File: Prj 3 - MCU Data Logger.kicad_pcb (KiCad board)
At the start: 2 copper layers, 0 parts

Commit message: Setup PCB New
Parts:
- added BT1: Battery, Connector_PinHeader_2.54mm:PinHeader_1x02_P2.54mm_Vertical, F.Cu at (154.9, 110.3)
- added C1: 0.1uF, Capacitor_SMD:C_0805_2012Metric, F.Cu at (177.2, 100.1)
- added C2: 22pF, Capacitor_SMD:C_0805_2012Metric, F.Cu at (177.2, 103.1)
- added C3: 22pF, Capacitor_SMD:C_0805_2012Metric, F.Cu at (177.2, 106.1)
- added C4: 0.1uF, Capacitor_SMD:C_0805_2012Metric, F.Cu at (177.2, 109.1)
- added C5: 100nF, Capacitor_SMD:C_0805_2012Metric, F.Cu at (177.2, 112.1)
- added D1: LED, LED_SMD:LED_0805_2012Metric, F.Cu at (181.7, 100.1)
- added D2: LED, LED_SMD:LED_0805_2012Metric, F.Cu at (181.7, 103.1)
- added H1: MountingHole, MountingHole:MountingHole_2.1mm, F.Cu at (155.5, 87.9)
- added H2: MountingHole, MountingHole:MountingHole_2.1mm, F.Cu at (155.5, 93.6)
- added H3: MountingHole, MountingHole:MountingHole_2.1mm, F.Cu at (155.5, 99.4)
- added H4: MountingHole, MountingHole:MountingHole_2.1mm, F.Cu at (155.5, 105.1)
- added J1: Conn_01x04_Pin, Connector_PinHeader_2.54mm:PinHeader_1x04_P2.54mm_Vertical, F.Cu at (192.8, 87.3)
- added J2: Conn_01x09_Pin, Connector_PinHeader_2.54mm:PinHeader_1x09_P2.54mm_Vertical, F.Cu at (188.2, 87.3)
- added J3: Conn_01x04_Pin, Connector_PinHeader_2.54mm:PinHeader_1x04_P2.54mm_Vertical, F.Cu at (197.5, 87.3)
- added J4: Conn_02x03_Odd_Even, Connector_PinHeader_2.54mm:PinHeader_2x03_P2.54mm_Vertical, F.Cu at (192.8, 99.6)
- added R1: 10k, Resistor_SMD:R_0805_2012Metric, F.Cu at (160.5, 86.5)
- added R2: 10k, Resistor_SMD:R_0805_2012Metric, F.Cu at (160.5, 89.4)
- added R3: 4.7k, Resistor_SMD:R_0805_2012Metric, F.Cu at (160.5, 92.4)
- added R4: 4.7k, Resistor_SMD:R_0805_2012Metric, F.Cu at (160.5, 95.3)
- added R5: 330, Resistor_SMD:R_0805_2012Metric, F.Cu at (160.5, 98.3)
- added R6: 10k, Resistor_SMD:R_0805_2012Metric, F.Cu at (160.5, 101.2)
- added R7: 330, Resistor_SMD:R_0805_2012Metric, F.Cu at (160.5, 104.2)
- added U1: 24LC1025, Package_SO:SOIC-8_5.23x5.23mm_P1.27mm, F.Cu at (167.9, 88.4)
- added U2: 24LC1025, Package_SO:SOIC-8_5.23x5.23mm_P1.27mm, F.Cu at (167.9, 95.2)
- added U3: DS1337S_, DS1337S:DS1337S, F.Cu at (167.9, 113.2)
- added U4: ATMEGA328P-AU, ATMEGA328P-AU:ATMEGA328P-AU, F.Cu at (169.3, 104.2)
- added Y1: 32.768 KHz, Crystal:Crystal_SMD_5032-2Pin_5.0x3.2mm_HandSoldering, F.Cu at (178.2, 87.4)
- added Y2: 16MHz, Crystal:Crystal_SMD_5032-2Pin_5.0x3.2mm_HandSoldering, F.Cu at (178.2, 92.3)

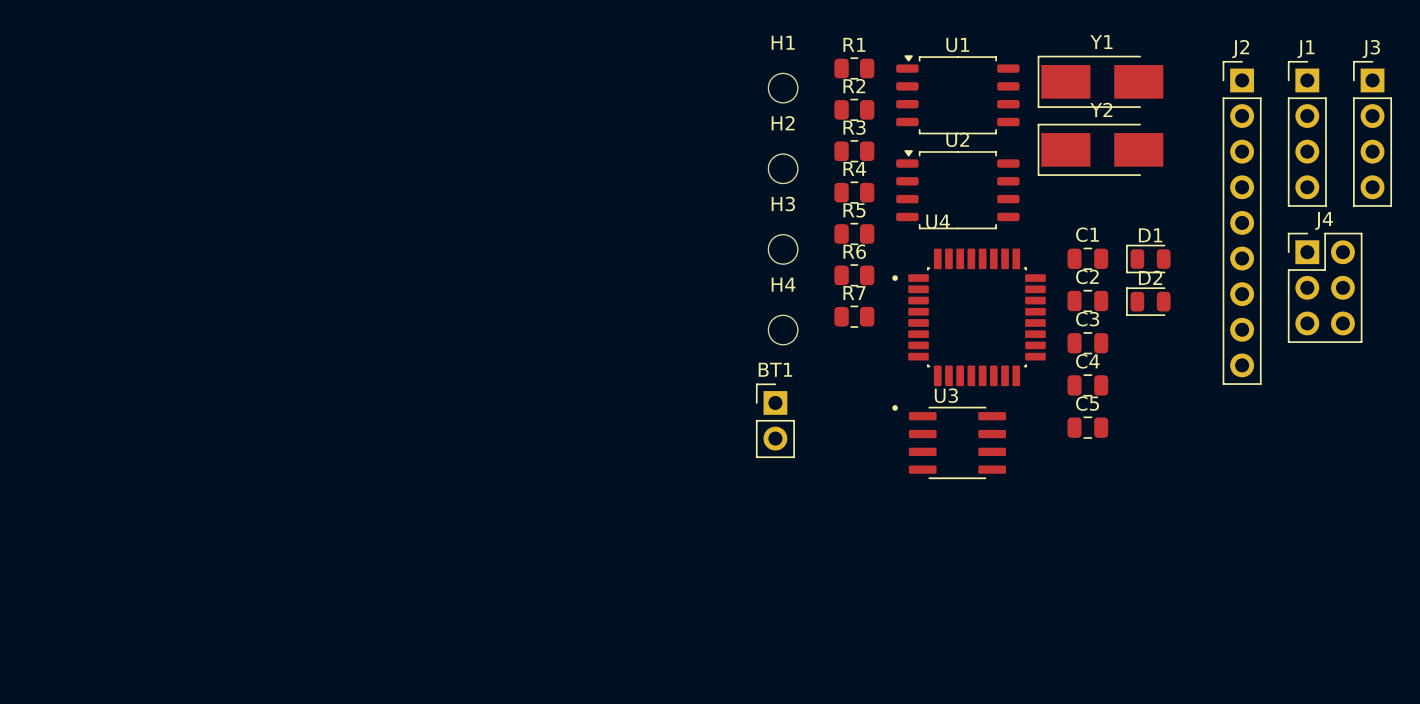
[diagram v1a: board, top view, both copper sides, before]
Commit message: Arranged placeholders
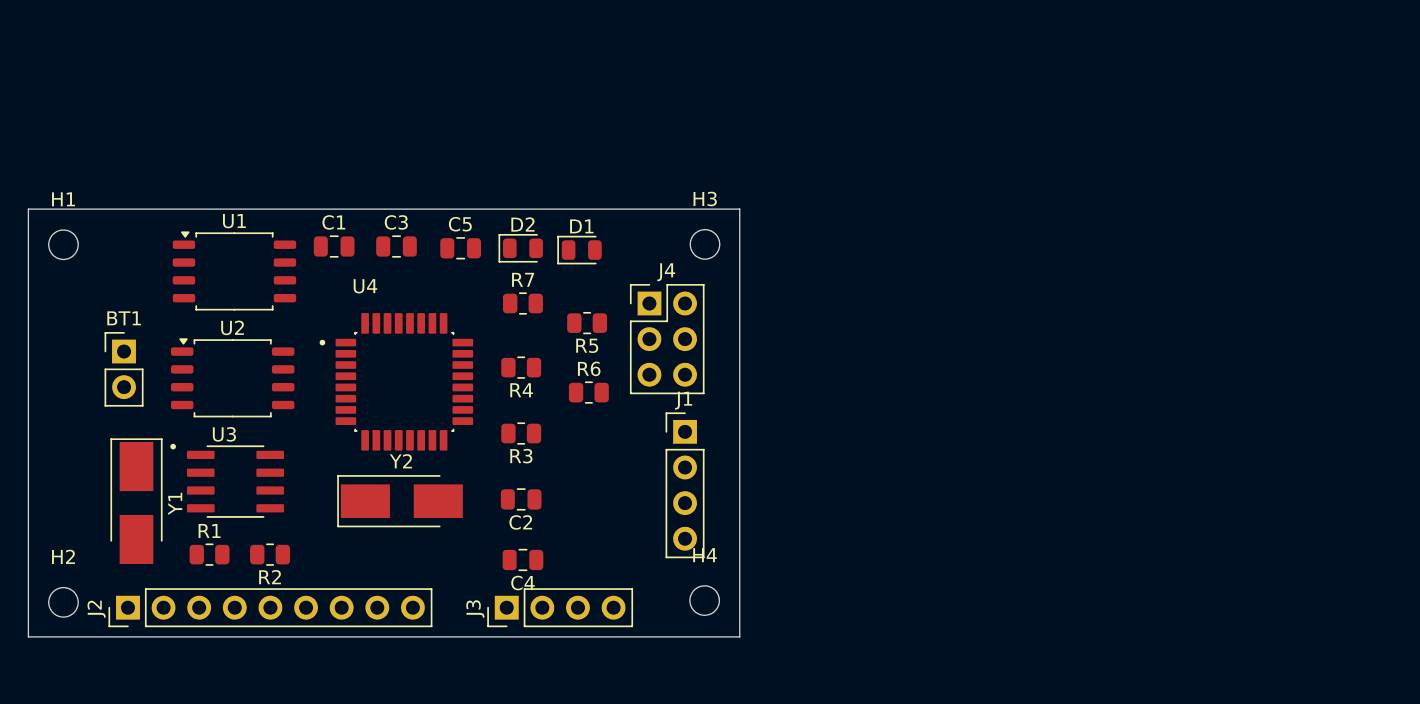
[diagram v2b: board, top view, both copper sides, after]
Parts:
- moved J2 87.9 mm to (108.7, 124.9), turned to 90 degrees
- moved Y1 75.1 mm to (109.3, 117.5), turned to -90 degrees
- moved J3 72.3 mm to (135.7, 124.9), turned to 90 degrees
- moved H2 59.9 mm to (104.1, 124.6)
- moved R1 57.6 mm to (114.6, 121.2)
- moved Y2 55.9 mm to (128.3, 117.3)
- moved C1 53.7 mm to (123.4, 99.2)
- moved U2 53.4 mm to (116.2, 108.6)
- moved U1 53.1 mm to (116.3, 101.0)
- moved H1 52.5 mm to (104.1, 99.1)
- moved R2 52.4 mm to (118.9, 121.2), turned to 180 degrees
- moved U3 51.6 mm to (116.4, 116.0)
- moved J1 51.0 mm to (148.5, 112.4)
- moved C3 49.8 mm to (127.9, 99.2)
- moved J4 47.1 mm to (145.9, 103.3)
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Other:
- board outline added: 50.7 x 30.5 mm

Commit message: Routing done except gnd and vcc
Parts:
- moved U2 7.49 mm to (116.1, 101.1)
- moved U1 7.37 mm to (116.2, 108.3)
- moved J2 2.01 mm to (110.7, 124.9)
- moved R6 1.78 mm to (141.5, 107.8)
- moved R5 1.40 mm to (141.4, 103.3), turned to 0 degrees
- moved U4 0.21 mm to (128.7, 108.8)
- turned Y2 to 180 degrees
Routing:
- net /Vcc: track 0.00 -> 129.0 mm, vias 0 -> 3
- net /SCK: track 0.00 -> 89.4 mm, vias 0 -> 3
- net Net-(BT1-+): track 0.00 -> 76.2 mm, vias 0 -> 5
- net /SDA: track 0.00 -> 61.5 mm, vias 0 -> 2
- net GND: track 0.00 -> 57.6 mm, vias 0 -> 3
- net /TX: track 0.00 -> 31.3 mm, vias 0 -> 1
- net /RX: track 0.00 -> 29.1 mm, vias 0 -> 1
- net /D2: track 0.00 -> 28.4 mm, vias 0 -> 1
- net /D3: track 0.00 -> 28.3 mm
- net Net-(U4-PB7): track 0.00 -> 26.2 mm, vias 0 -> 2
- net /D4: track 0.00 -> 25.2 mm
- net /MOSI: track 0.00 -> 24.4 mm
- net /RESET: track 0.00 -> 22.8 mm, vias 0 -> 4
- net Net-(U4-PB6): track 0.00 -> 19.9 mm
- net /MISO: track 0.00 -> 19.6 mm, vias 0 -> 1
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
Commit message: Routing completed
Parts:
- moved H2 3.54 mm to (106.5, 127.2)
- moved H1 3.21 mm to (106.4, 96.8)
- moved H4 2.97 mm to (150.8, 127.2)
- moved H3 2.44 mm to (150.8, 96.8)
- moved Y1 0.76 mm to (108.6, 117.5)
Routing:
- net GND: track 57.6 -> 78.1 mm, vias 3 -> 9
- net /Vcc: track 129.0 -> 133.2 mm
- net Net-(BT1-+): track 76.2 -> 78.8 mm
- net Net-(U4-AREF): track 17.4 -> 19.2 mm
- net Net-(U4-PB7): track 26.2 -> 27.3 mm
- net Net-(U3-X2): track 8.00 -> 8.77 mm
- net Net-(U3-X1): track 4.93 -> 5.69 mm
- added copper zone on F.Cu, net /Vcc
- added copper zone on B.Cu, net GND
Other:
- board size 50.7 x 30.5 mm -> 49.6 x 35.6 mm

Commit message: Fixed outstanding issues
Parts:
- moved C4 1.34 mm to (136.9, 120.2)
- moved BT1 0.72 mm to (108.7, 106.0)
- moved C2 0.63 mm to (136.9, 116.6)
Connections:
- BT1 pad 1: Net-(BT1-+) -> /Vcc
- C5 pad 1: Net-(BT1-+) -> /Vcc
- D2 pad 2: Net-(BT1-+) -> /Vcc
- U4 pad 18: Net-(BT1-+) -> /Vcc
- U4 pad 4: Net-(BT1-+) -> /Vcc
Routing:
- net /Vcc: track 133.2 -> 217.2 mm, vias 3 -> 8
- net Net-(BT1-+): track 78.8 -> 0.00 mm, vias 5 -> 0
- net Net-(U4-AREF): track 19.2 -> 17.5 mm
- net GND: track 78.1 -> 78.7 mm
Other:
- board text added: "2"
- board text added: "3"
- board text added: "4"
- board text added: "5"
- board text added: "6"
- board text added: "7"
- board text added: "8"
- board text added: "GND"
- board text added: "GPIO"
- board text added: "I2C"
- board text added: "ICSP"
- board text added: "ICSP MISO | VCC SCK | MOSI RESET | GND"
- board text added: "RX"
- board text added: "SCK"
- board text added: "SDA"
- board text added: "TX"
- board text added: "VCC"

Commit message: Completed 2 layer PCB Project
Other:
- board text added: "0.2000 mm / 0.0000 mm"
- board text added: "0.3000 mm"
- board text added: "1.6000 mm"
- board text added: "49.6040 mm x 35.6040 mm"
- board text added: "BOARD CHARACTERISTICS"
- board text added: "Board Thickness:"
- board text added: "Board overall dimensions:"
- board text added: "Castellated pads:"
- board text added: "Copper Finish:"
- board text added: "Copper Layer Count:"
- board text added: "Edge card connectors:"
- board text added: "Impedance Control:"
- board text added: "Min hole diameter:"
- board text added: "Min track/spacing:"
- board text added: "No"
- board text added: "None"
- board text added: "Plated Board Edge:"
